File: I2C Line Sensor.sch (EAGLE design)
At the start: 31 parts, among them U1 ADS7830

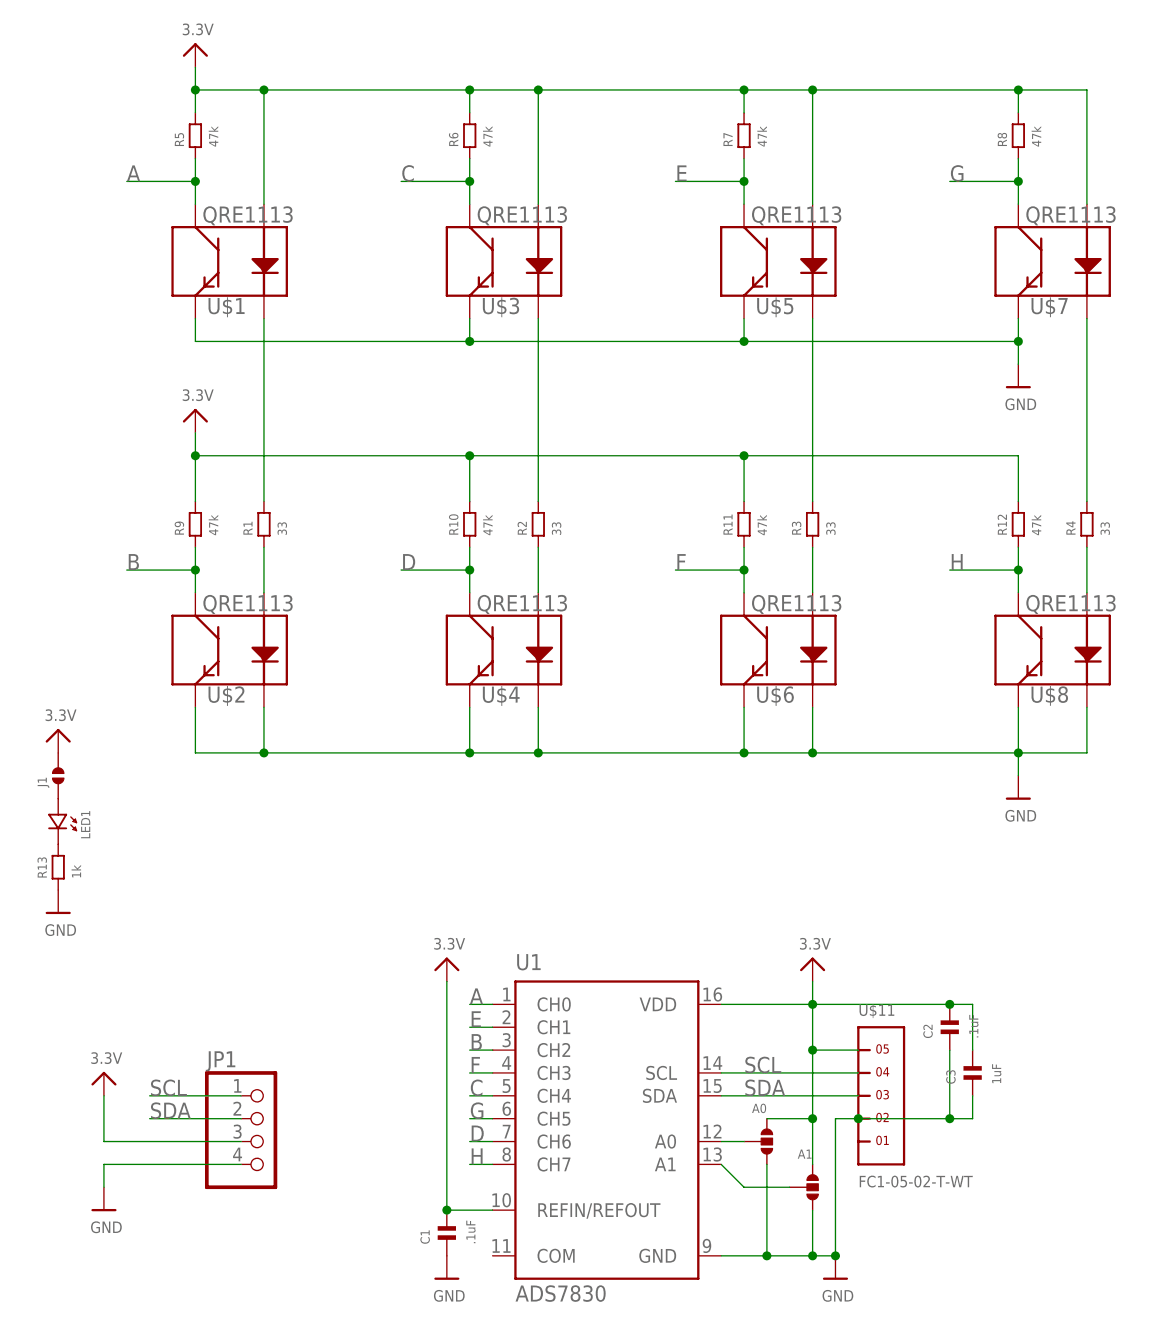
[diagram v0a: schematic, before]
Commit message: Cleaned up I2C Line Sensor. Added 5 ohm resistor as per datasheet. Updated footprints and removed Zero Force Connector.
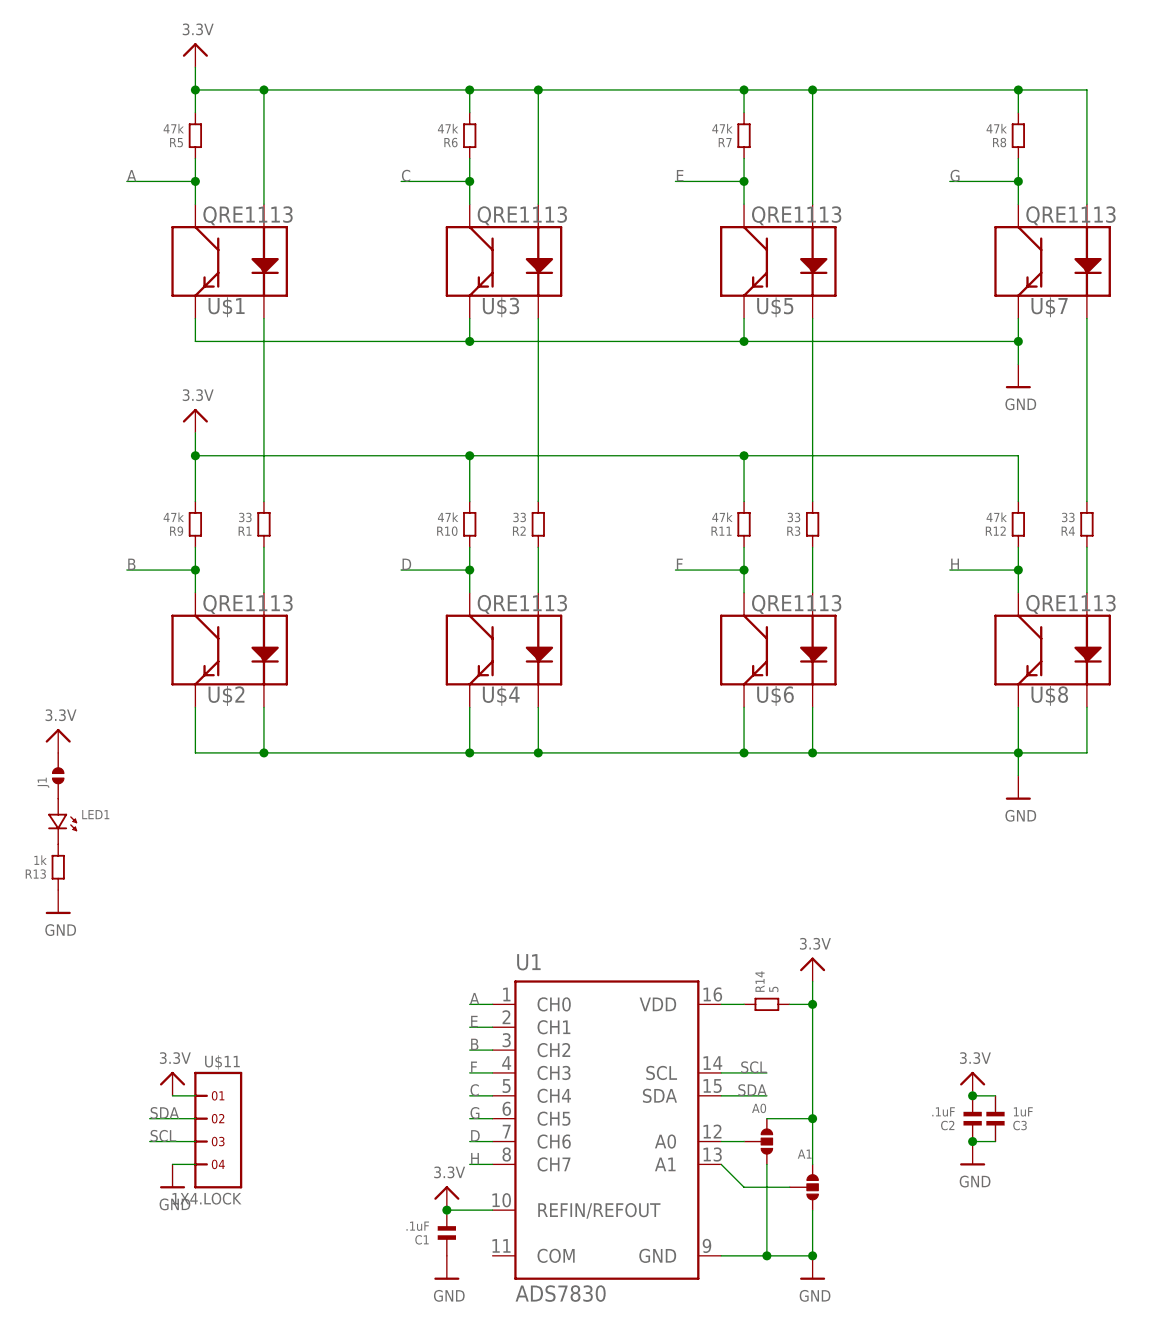
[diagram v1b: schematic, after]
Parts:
- removed JP1: (no value), microbuilder:HEADER-1X4
- added R14: 5, standardparts:RESISTOR.0603
- C1, C2, C3: device .standardparts:CAPACITOR.0603 -> standardparts:CAPACITOR.0603
- LED1: device .standardparts:LED.0603 -> standardparts:LED.0603
- R1, R10, R11, R12, R13, R2, R3, R4, R5, R6, R7, R8, R9: device .standardparts:RESISTOR.0603 -> standardparts:RESISTOR.0603
- U$11: value FC1-05-02-T-WT -> 1X4.LOCK; device samtec:FC1-05-02-T-WT -> headers(.1in):1X4.LOCK
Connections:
- new net N$15: R14.1, U1.VDD
- net 3.3V: now also R14.2, U$11.1; no longer JP1.3, U$11.5, U1.VDD
- net GND: now also U$11.4; no longer JP1.4, U$11.2
- net SCL: now also U$11.3; no longer JP1.1, U$11.4
- net SDA: now also U$11.2; no longer JP1.2, U$11.3
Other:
- moved on the sheet: C2, C3

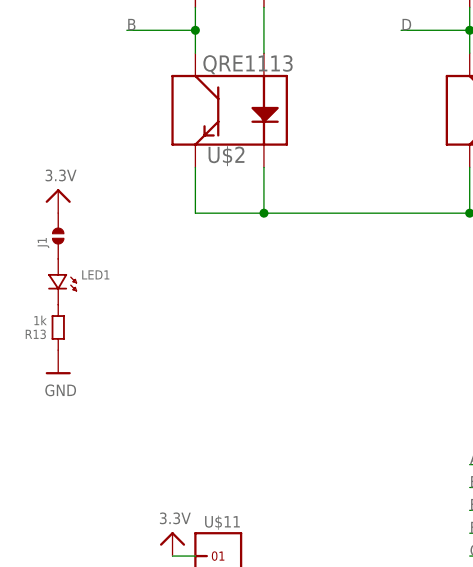
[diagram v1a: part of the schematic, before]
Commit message: Cleaned up layout of I2C Mini Line Sensor and I2C Line Sensor Also geenerated preview images
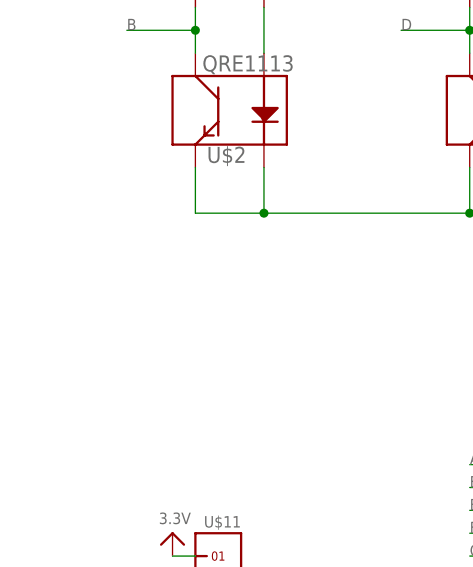
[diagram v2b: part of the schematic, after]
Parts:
- removed J1: (no value), .solderjumper:SOLDERJUMPER.2.MED
- removed LED1: (no value), standardparts:LED.0603
- removed R13: 1k, standardparts:RESISTOR.0603
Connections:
- removed net N$11: LED1.2, R13.2
- removed net N$12: J1.1, LED1.1
- net 3.3V: no longer J1.2
- net GND: no longer R13.1
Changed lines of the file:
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@@
 <grid distance="0.1" unitdist="inch" unit="inch" style="lines" multiple="1" display="no" altdistance="0.01" altunitdist="inch" altunit="inch"/>
 <layers>
-<layer number="1" name="Top" color="4" fill="1" visible="yes" active="no"/>
-<layer number="16" name="Bottom" color="1" fill="1" visible="yes" active="no"/>
-<layer number="17" name="Pads" color="2" fill="1" visible="yes" active="no"/>
-<layer number="18" name="Vias" color="2" fill="1" visible="yes" active="no"/>
-<layer number="19" name="Unrouted" color="6" fill="1" visible="yes" active="no"/>
-<layer number="20" name="Dimension" color="15" fill="1" visible="yes" active="no"/>
-<layer number="21" name="tPlace" color="7" fill="1" visible="yes" active="no"/>
-<layer number="22" name="bPlace" color="7" fill="1" visible="yes" active="no"/>
-<layer number="23" name="tOrigins" color="15" fill="1" visible="yes" active="no"/>
-<layer number="24" name="bOrigins" color="15" fill="1" visible="yes" active="no"/>
-<layer number="25" name="tNames" color="7" fill="1" visible="yes" active="no"/>
-<layer number="26" name="bNames" color="7" fill="1" visible="yes" active="no"/>
-<layer number="27" name="tValues" color="7" fill="1" visible="yes" active="no"/>
-<layer number="28" name="bValues" color="7" fill="1" visible="yes" active="no"/>
+<layer number="1" name="Top" color="4" fill="1" visible="no" active="no"/>
+<layer number="16" name="Bottom" color="1" fill="1" visible="no" active="no"/>
+<layer number="17" name="Pads" color="2" fill="1" visible="no" active="no"/>
+<layer number="18" name="Vias" color="2" fill="1" visible="no" active="no"/>
+<layer number="19" name="Unrouted" color="6" fill="1" visible="no" active="no"/>
+<layer number="20" name="Dimension" color="15" fill="1" visible="no" active="no"/>
+<layer number="21" name="tPlace" color="7" fill="1" visible="no" active="no"/>
+<layer number="22" name="bPlace" color="7" fill="1" visible="no" active="no"/>
+<layer number="23" name="tOrigins" color="15" fill="1" visible="no" active="no"/>
+<layer number="24" name="bOrigins" color="15" fill="1" visible="no" active="no"/>
+<layer number="25" name="tNames" color="7" fill="1" visible="no" active="no"/>
+<layer number="26" name="bNames" color="7" fill="1" visible="no" active="no"/>
+<layer number="27" name="tValues" color="7" fill="1" visible="no" active="no"/>
+<layer number="28" name="bValues" color="7" fill="1" visible="no" active="no"/>
 <layer number="29" name="tStop" color="7" fill="3" visible="no" active="no"/>
 <layer number="30" name="bStop" color="7" fill="6" visible="no" active="no"/>
@@
 <layer number="35" name="tGlue" color="7" fill="4" visible="no" active="no"/>
 <layer number="36" name="bGlue" color="7" fill="5" visible="no" active="no"/>
-<layer number="37" name="tTest" color="7" fill="1" visible="yes" active="no"/>
-<layer number="38" name="bTest" color="7" fill="1" visible="yes" active="no"/>
+<layer number="37" name="tTest" color="7" fill="1" visible="no" active="no"/>
+<layer number="38" name="bTest" color="7" fill="1" visible="no" active="no"/>
 <layer number="39" name="tKeepout" color="4" fill="11" visible="no" active="no"/>
 <layer number="40" name="bKeepout" color="1" fill="11" visible="no" active="no"/>
@@
 <layer number="44" name="Drills" color="7" fill="1" visible="no" active="no"/>
 <layer number="45" name="Holes" color="7" fill="1" visible="no" active="no"/>
-<layer number="46" name="Milling" color="3" fill="1" visible="yes" active="no"/>
-<layer number="47" name="Measures" color="7" fill="1" visible="yes" active="no"/>
-<layer number="48" name="Document" color="7" fill="1" visible="yes" active="no"/>
-<layer number="49" name="Reference" color="7" fill="1" visible="yes" active="no"/>
-<layer number="50" name="dxf" color="7" fill="1" visible="yes" active="no"/>
-<layer number="51" name="tDocu" color="7" fill="1" visible="yes" active="no"/>
-<layer number="52" name="bDocu" color="7" fill="1" visible="yes" active="no"/>
-<layer number="53" name="tGND_GNDA" color="7" fill="9" visible="yes" active="no"/>
-<layer number="54" name="bGND_GNDA" color="1" fill="9" visible="yes" active="no"/>
-<layer number="56" name="wert" color="7" fill="1" visible="yes" active="no"/>
+<layer number="46" name="Milling" color="3" fill="1" visible="no" active="no"/>
+<layer number="47" name="Measures" color="7" fill="1" visible="no" active="no"/>
+<layer number="48" name="Document" color="7" fill="1" visible="no" active="no"/>
+<layer number="49" name="Reference" color="7" fill="1" visible="no" active="no"/>
+<layer number="50" name="dxf" color="7" fill="1" visible="no" active="no"/>
+<layer number="51" name="tDocu" color="7" fill="1" visible="no" active="no"/>
+<layer number="52" name="bDocu" color="7" fill="1" visible="no" active="no"/>
+<layer number="53" name="tGND_GNDA" color="7" fill="9" visible="no" active="no"/>
+<layer number="54" name="bGND_GNDA" color="1" fill="9" visible="no" active="no"/>
+<layer number="56" name="wert" color="7" fill="1" visible="no" active="no"/>
 <layer number="91" name="Nets" color="2" fill="1" visible="yes" active="yes"/>
 <layer number="92" name="Busses" color="1" fill="1" visible="yes" active="yes"/>
@@
 <part name="C3" library="standardparts" deviceset="CAPACITOR" device=".0603" value="1uF"/>
 <part name="U$9" library="microbuilder" deviceset="GND" device=""/>
-<part name="LED1" library="standardparts" deviceset="LED" device=".0603"/>
-<part name="R13" library="standardparts" deviceset="RESISTOR" device=".0603" value="1k"/>
-<part name="U$10" library="microbuilder" deviceset="GND" device=""/>
-<part name="U$24" library="microbuilder" deviceset="3.3V" device=""/>
-<part name="J1" library=".solderjumper" deviceset="SOLDERJUMPER.2" device=".MED"/>
 <part name="U$11" library="headers(.1in)" deviceset="1X4" device=".LOCK" value="1X4.LOCK"/>
 <part name="R14" library="standardparts" deviceset="RESISTOR" device=".0603" value="5"/>
@@
 <instance part="C3" gate="G$1" x="114.3" y="48.26" rot="MR90"/>
 <instance part="U$9" gate="G$1" x="53.34" y="30.48"/>
-<instance part="LED1" gate="G$1" x="10.16" y="81.28" rot="R270"/>
-<instance part="R13" gate="G$1" x="10.16" y="76.2" rot="R90"/>
-<instance part="U$10" gate="G$1" x="10.16" y="71.12"/>
-<instance part="U$24" gate="G$1" x="10.16" y="88.9"/>
-<instance part="J1" gate="G$1" x="10.16" y="86.36" rot="R90"/>
 <instance part="U$11" gate="G$1" x="27.94" y="45.72" rot="MR0"/>
 <instance part="R14" gate="G$1" x="88.9" y="60.96"/>
@@
 <pinref part="C1" gate="G$1" pin="1"/>
 <pinref part="U$9" gate="G$1" pin="GND"/>
-</segment>
-<segment>
-<pinref part="R13" gate="G$1" pin="1"/>
-<pinref part="U$10" gate="G$1" pin="GND"/>
 </segment>
 <segment>
@@
 </segment>
 <segment>
-<pinref part="J1" gate="G$1" pin="2"/>
-<pinref part="U$24" gate="G$1" pin="3.3V"/>
-</segment>
-<segment>
 <pinref part="U$16" gate="G$1" pin="3.3V"/>
 <pinref part="U$11" gate="G$1" pin="1"/>
@@
 </segment>
 </net>
-<net name="N$11" class="0">
-<segment>
-<pinref part="LED1" gate="G$1" pin="2"/>
-<pinref part="R13" gate="G$1" pin="2"/>
-</segment>
-</net>
-<net name="N$12" class="0">
-<segment>
-<pinref part="LED1" gate="G$1" pin="1"/>
-<pinref part="J1" gate="G$1" pin="1"/>
-</segment>
-</net>

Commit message: Regenerate screnshots
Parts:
- R13: value 5 -> 5.1
- renumbered R14 to R13
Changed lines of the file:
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@@
 <part name="U$9" library="microbuilder" deviceset="GND" device=""/>
 <part name="U$11" library="headers(.1in)" deviceset="1X4" device=".LOCK" value="1X4.LOCK"/>
-<part name="R14" library="standardparts" deviceset="RESISTOR" device=".0603" value="5"/>
+<part name="R13" library="standardparts" deviceset="RESISTOR" device=".0603" value="5.1"/>
 <part name="U$12" library="microbuilder" deviceset="3.3V" device=""/>
 <part name="U$13" library="microbuilder" deviceset="GND" device=""/>
@@
 <instance part="U$9" gate="G$1" x="53.34" y="30.48"/>
 <instance part="U$11" gate="G$1" x="27.94" y="45.72" rot="MR0"/>
-<instance part="R14" gate="G$1" x="88.9" y="60.96"/>
+<instance part="R13" gate="G$1" x="88.9" y="60.96"/>
 <instance part="U$12" gate="G$1" x="111.76" y="50.8"/>
 <instance part="U$13" gate="G$1" x="111.76" y="43.18"/>
@@
 <wire x1="88.9" y1="48.26" x2="93.98" y2="48.26" width="0.1524" layer="91"/>
 <junction x="93.98" y="48.26"/>
-<pinref part="R14" gate="G$1" pin="2"/>
+<pinref part="R13" gate="G$1" pin="2"/>
 <wire x1="91.44" y1="60.96" x2="93.98" y2="60.96" width="0.1524" layer="91"/>
 <junction x="93.98" y="60.96"/>
@@
 <segment>
 <pinref part="U1" gate="G$1" pin="VDD"/>
-<pinref part="R14" gate="G$1" pin="1"/>
+<pinref part="R13" gate="G$1" pin="1"/>
 <wire x1="83.82" y1="60.96" x2="86.36" y2="60.96" width="0.1524" layer="91"/>
 </segment>

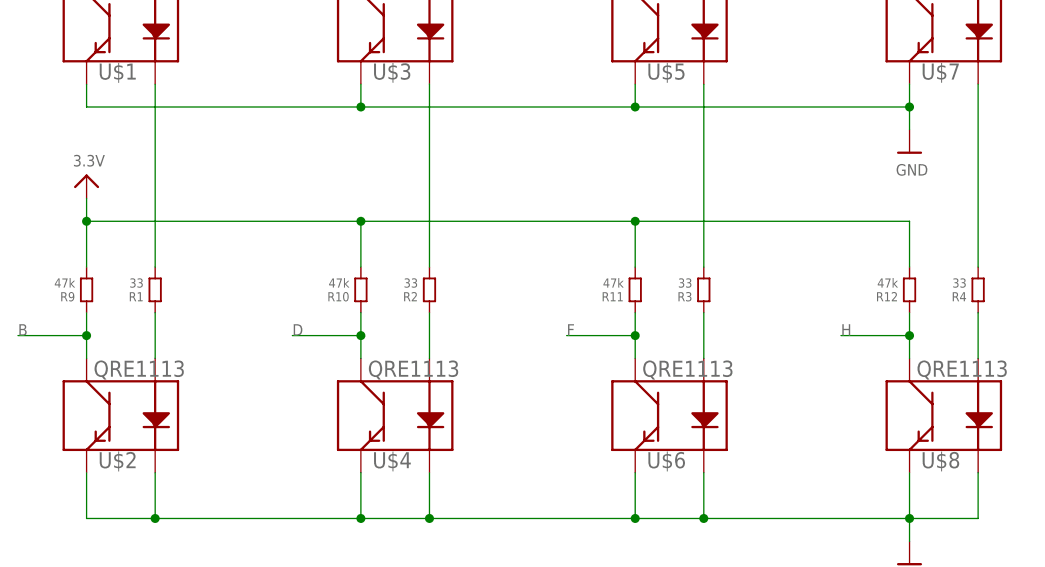
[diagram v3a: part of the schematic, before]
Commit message: Changd R[1-4] values to 51 ohms instead of 33 ohms. PCBs should no longer heat up due to current draw.
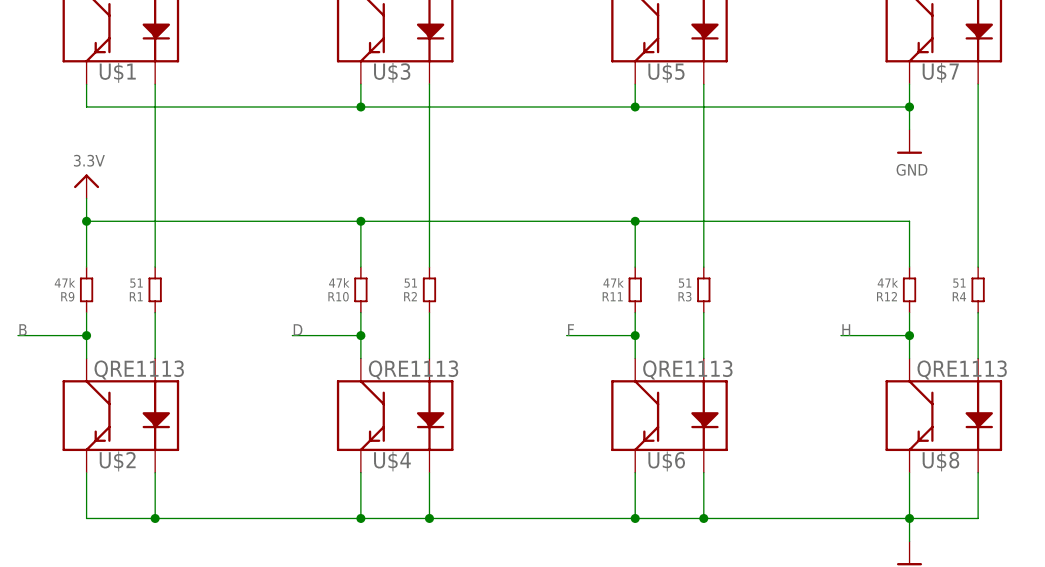
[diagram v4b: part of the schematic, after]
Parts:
- R1, R2, R3, R4: value 33 -> 51
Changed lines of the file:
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@@
 <part name="U$18" library="microbuilder" deviceset="3.3V" device=""/>
 <part name="U$19" library="thinkmaketest" deviceset="A4_LAYOUT" device=""/>
-<part name="R1" library="standardparts" deviceset="RESISTOR" device=".0603" value="33"/>
-<part name="R2" library="standardparts" deviceset="RESISTOR" device=".0603" value="33"/>
-<part name="R3" library="standardparts" deviceset="RESISTOR" device=".0603" value="33"/>
-<part name="R4" library="standardparts" deviceset="RESISTOR" device=".0603" value="33"/>
+<part name="R1" library="standardparts" deviceset="RESISTOR" device=".0603" value="51"/>
+<part name="R2" library="standardparts" deviceset="RESISTOR" device=".0603" value="51"/>
+<part name="R3" library="standardparts" deviceset="RESISTOR" device=".0603" value="51"/>
+<part name="R4" library="standardparts" deviceset="RESISTOR" device=".0603" value="51"/>
 <part name="R5" library="standardparts" deviceset="RESISTOR" device=".0603" value="47k"/>
 <part name="R6" library="standardparts" deviceset="RESISTOR" device=".0603" value="47k"/>
